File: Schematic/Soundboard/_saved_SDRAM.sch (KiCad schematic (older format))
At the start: 2 parts, among them U1 STM32f429IIT6-units, U8 IS42S16400J-xC

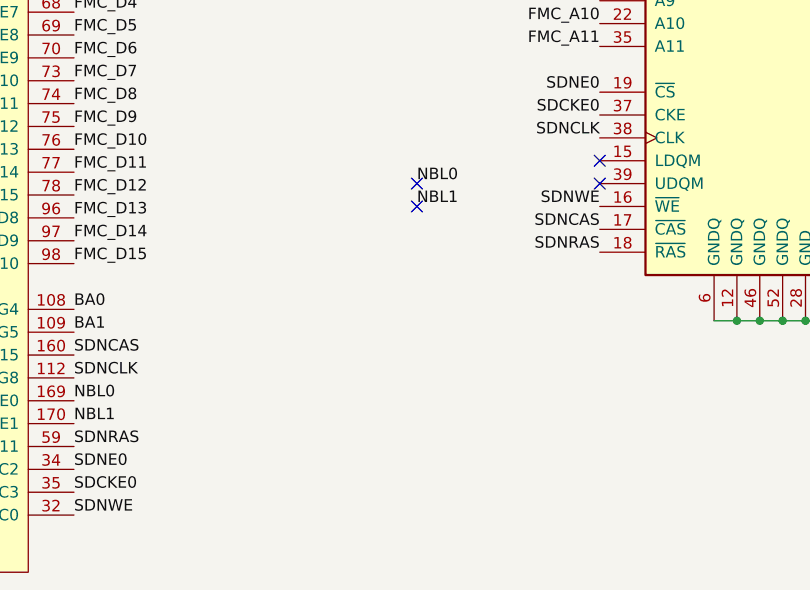
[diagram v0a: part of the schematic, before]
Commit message: Complete part selection. Start connections
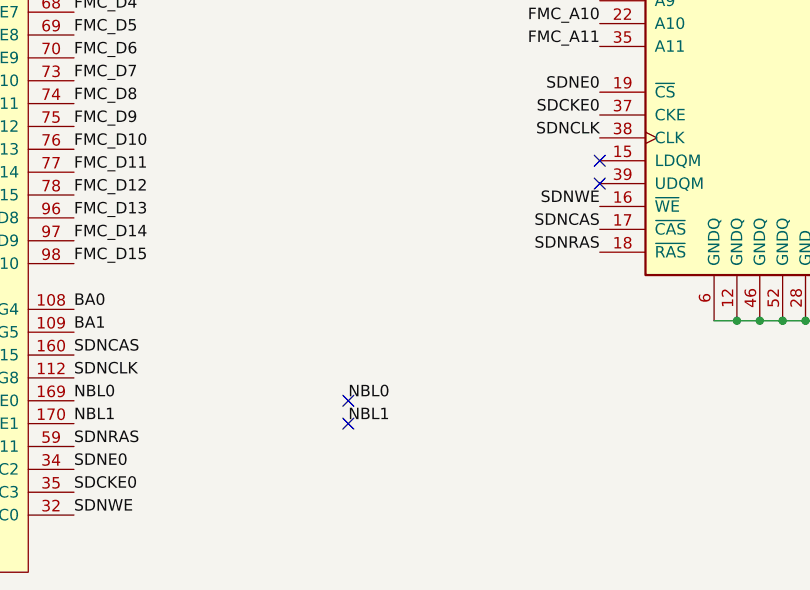
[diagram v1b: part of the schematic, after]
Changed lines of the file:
@@
 Text Label 5100 4150 2    50   ~ 0
 SDNCLK
-Text Label 4300 4350 0    50   ~ 0
+Text Label 4000 5300 0    50   ~ 0
 NBL0
-Text Label 4300 4450 0    50   ~ 0
+Text Label 4000 5400 0    50   ~ 0
 NBL1
 Text Label 5100 4650 2    50   ~ 0
@@
 	1    0    0    -1
 $EndComp
-NoConn ~ 4300 4450
-NoConn ~ 4300 4350
+NoConn ~ 4000 5400
+NoConn ~ 4000 5300
 NoConn ~ 5100 4350
 NoConn ~ 5100 4250
